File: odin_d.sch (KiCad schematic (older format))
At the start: 27 parts, among them J1 Conn_01x03, Q4 Q_NPN_BEC, Q5 Q_NPN_BEC, T1 BT136S

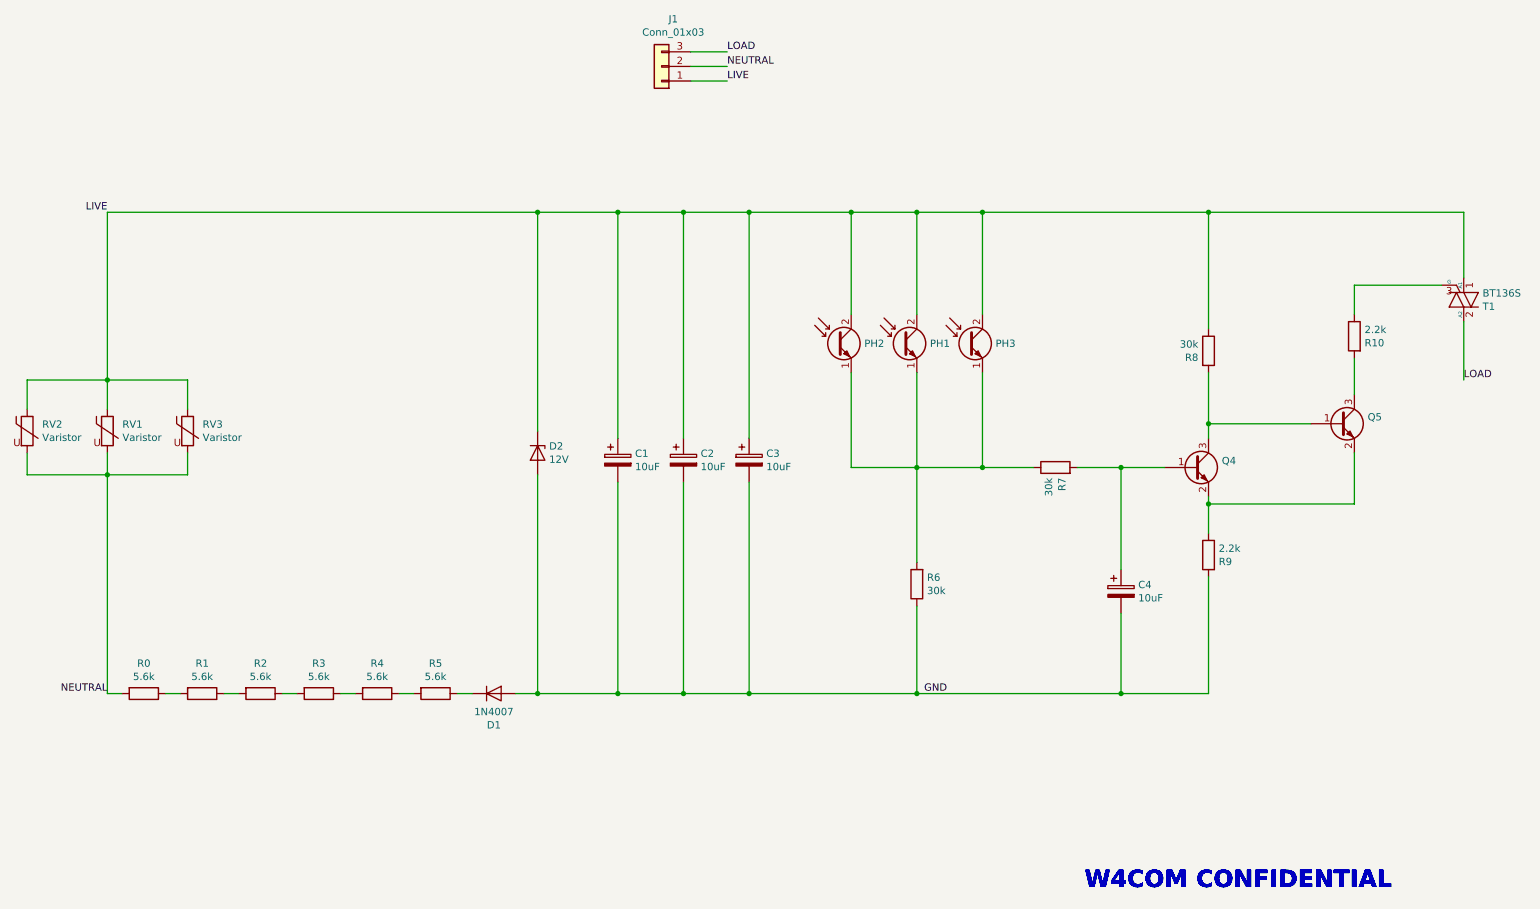
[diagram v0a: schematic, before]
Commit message: Added 1210 footprint resistor for 110/220 VAC version
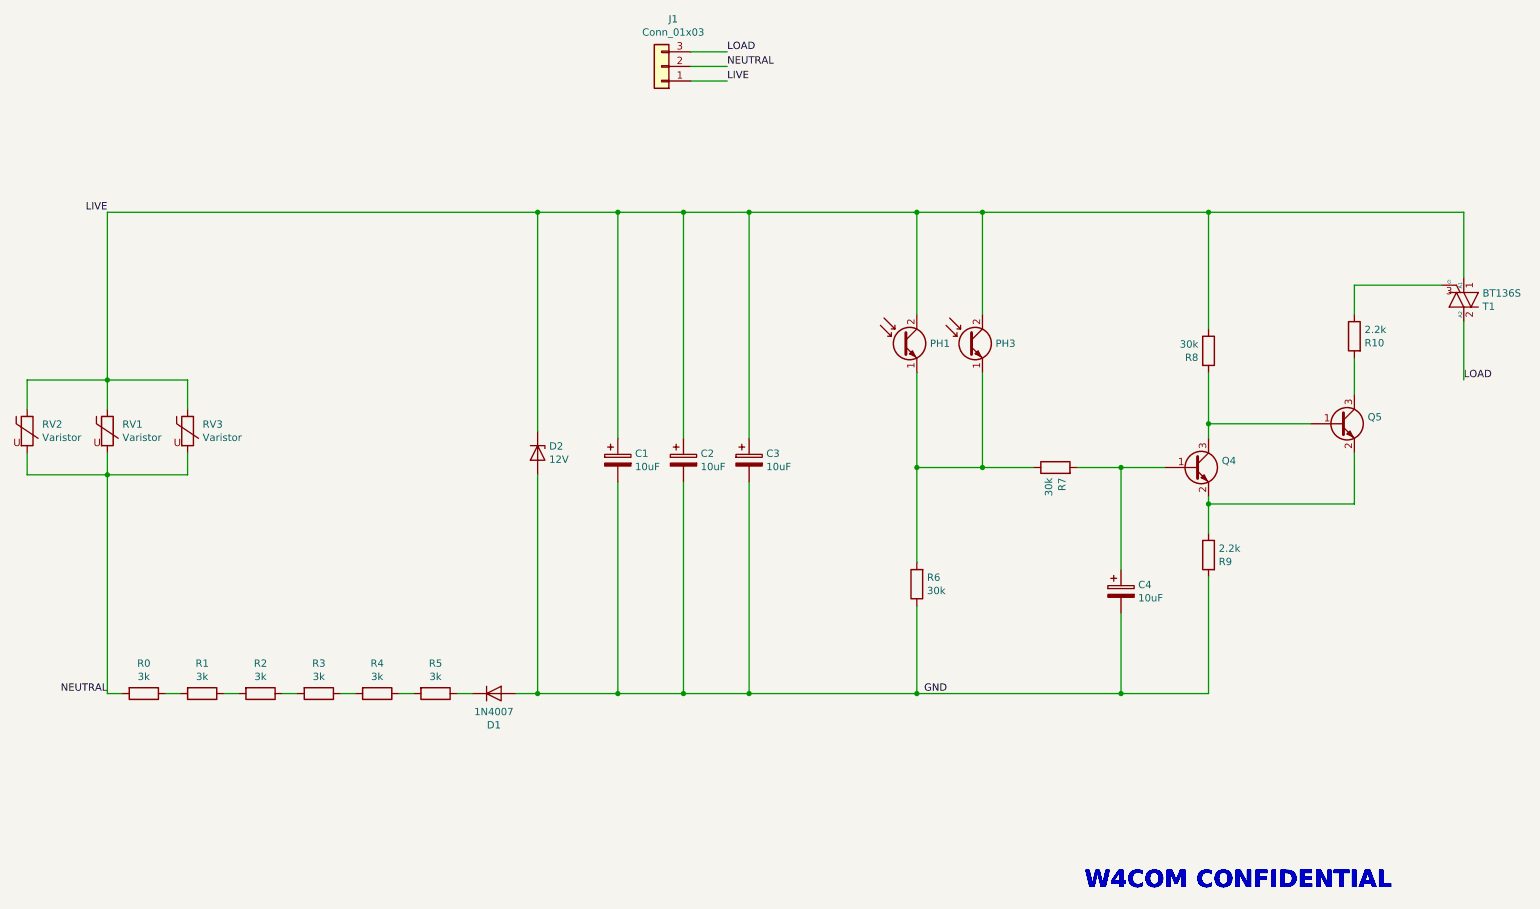
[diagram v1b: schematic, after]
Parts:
- removed PH2: Q_Photo_NPN_EC, Resistor_SMD:R_0603_1608Metric, symbol Device:Q_Photo_NPN_EC
- R0, R1, R2, R3, R4, R5: value 5.6k -> 3k; footprint Resistor_SMD:R_1206_3216Metric -> Resistor_SMD:R_1210_3225Metric
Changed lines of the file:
@@
 EESchema Schematic File Version 4
-LIBS:odin_c-cache
+LIBS:odin_d-cache
 EELAYER 30 0
 EELAYER END
@@
 P 1600 5600
 F 0 "R0" V 1393 5600 50  0000 C CNN
-F 1 "5.6k" V 1484 5600 50  0000 C CNN
-F 2 "Resistor_SMD:R_1206_3216Metric" V 1530 5600 50  0001 C CNN
+F 1 "3k" V 1484 5600 50  0000 C CNN
+F 2 "Resistor_SMD:R_1210_3225Metric" V 1530 5600 50  0001 C CNN
 F 3 "~" H 1600 5600 50  0001 C CNN
 F 4 "0805W8J0473T5E" H 1600 5600 50  0001 C CNN "MPN"
@@
 P 2000 5600
 F 0 "R1" V 1793 5600 50  0000 C CNN
-F 1 "5.6k" V 1884 5600 50  0000 C CNN
-F 2 "Resistor_SMD:R_1206_3216Metric" V 1930 5600 50  0001 C CNN
+F 1 "3k" V 1884 5600 50  0000 C CNN
+F 2 "Resistor_SMD:R_1210_3225Metric" V 1930 5600 50  0001 C CNN
 F 3 "~" H 2000 5600 50  0001 C CNN
 F 4 "0805W8J0473T5E" H 2000 5600 50  0001 C CNN "MPN"
@@
 Wire Wire Line
 	10500 2800 9900 2800
-$Comp
-L Device:Q_Photo_NPN_EC PH2
-U 1 1 5F8C2011
-P 6350 3200
-F 0 "PH2" H 6540 3200 50  0000 L CNN
-F 1 "Q_Photo_NPN_EC" H 6541 3155 50  0001 L CNN
-F 2 "Resistor_SMD:R_0603_1608Metric" H 6550 3300 50  0001 C CNN
-F 3 "~" H 6350 3200 50  0001 C CNN
-	1    6350 3200
-	1    0    0    -1
-$EndComp
 Wire Wire Line
 	1350 2300 1350 3450
@@
 Wire Wire Line
 	1350 3950 1350 4100
-Wire Wire Line
-	6450 2300 6450 3000
 Wire Wire Line
 	8300 4750 8300 4050
@@
 Wire Wire Line
 	6900 5000 6900 5600
-Wire Wire Line
-	6450 3400 6450 4050
 $Comp
 L Device:Q_NPN_BEC Q4
@@
 P 2400 5600
 F 0 "R2" V 2193 5600 50  0000 C CNN
-F 1 "5.6k" V 2284 5600 50  0000 C CNN
-F 2 "Resistor_SMD:R_1206_3216Metric" V 2330 5600 50  0001 C CNN
+F 1 "3k" V 2284 5600 50  0000 C CNN
+F 2 "Resistor_SMD:R_1210_3225Metric" V 2330 5600 50  0001 C CNN
 F 3 "~" H 2400 5600 50  0001 C CNN
 F 4 "0805W8J0473T5E" H 2400 5600 50  0001 C CNN "MPN"
@@
 P 2800 5600
 F 0 "R3" V 2593 5600 50  0000 C CNN
-F 1 "5.6k" V 2684 5600 50  0000 C CNN
-F 2 "Resistor_SMD:R_1206_3216Metric" V 2730 5600 50  0001 C CNN
+F 1 "3k" V 2684 5600 50  0000 C CNN
+F 2 "Resistor_SMD:R_1210_3225Metric" V 2730 5600 50  0001 C CNN
 F 3 "~" H 2800 5600 50  0001 C CNN
 F 4 "0805W8J0473T5E" H 2800 5600 50  0001 C CNN "MPN"
@@
 P 3200 5600
 F 0 "R4" V 2993 5600 50  0000 C CNN
-F 1 "5.6k" V 3084 5600 50  0000 C CNN
-F 2 "Resistor_SMD:R_1206_3216Metric" V 3130 5600 50  0001 C CNN
+F 1 "3k" V 3084 5600 50  0000 C CNN
+F 2 "Resistor_SMD:R_1210_3225Metric" V 3130 5600 50  0001 C CNN
 F 3 "~" H 3200 5600 50  0001 C CNN
 F 4 "0805W8J0473T5E" H 3200 5600 50  0001 C CNN "MPN"
@@
 P 3600 5600
 F 0 "R5" V 3393 5600 50  0000 C CNN
-F 1 "5.6k" V 3484 5600 50  0000 C CNN
-F 2 "Resistor_SMD:R_1206_3216Metric" V 3530 5600 50  0001 C CNN
+F 1 "3k" V 3484 5600 50  0000 C CNN
+F 2 "Resistor_SMD:R_1210_3225Metric" V 3530 5600 50  0001 C CNN
 F 3 "~" H 3600 5600 50  0001 C CNN
 F 4 "0805W8J0473T5E" H 3600 5600 50  0001 C CNN "MPN"
@@
 	7350 3400 7350 4050
 Wire Wire Line
-	6450 2300 6900 2300
-Wire Wire Line
-	5750 2300 6450 2300
-Wire Wire Line
 	3750 5600 3850 5600
 Wire Wire Line
@@
 Wire Wire Line
 	4300 5600 4850 5600
-Connection ~ 6450 2300
 Connection ~ 7350 2300
 Connection ~ 6900 5600
 Wire Wire Line
 	6900 3400 6900 4050
-Wire Wire Line
-	6450 4050 6900 4050
 Connection ~ 6900 4050
 Wire Wire Line
@@
 Wire Wire Line
 	1350 3450 1900 3450
+Wire Wire Line
+	5750 2300 6900 2300
 $EndSCHEMATC
